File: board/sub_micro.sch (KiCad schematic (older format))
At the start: 2 parts, among them J301 USB_B, U301 STM32F072CBTx

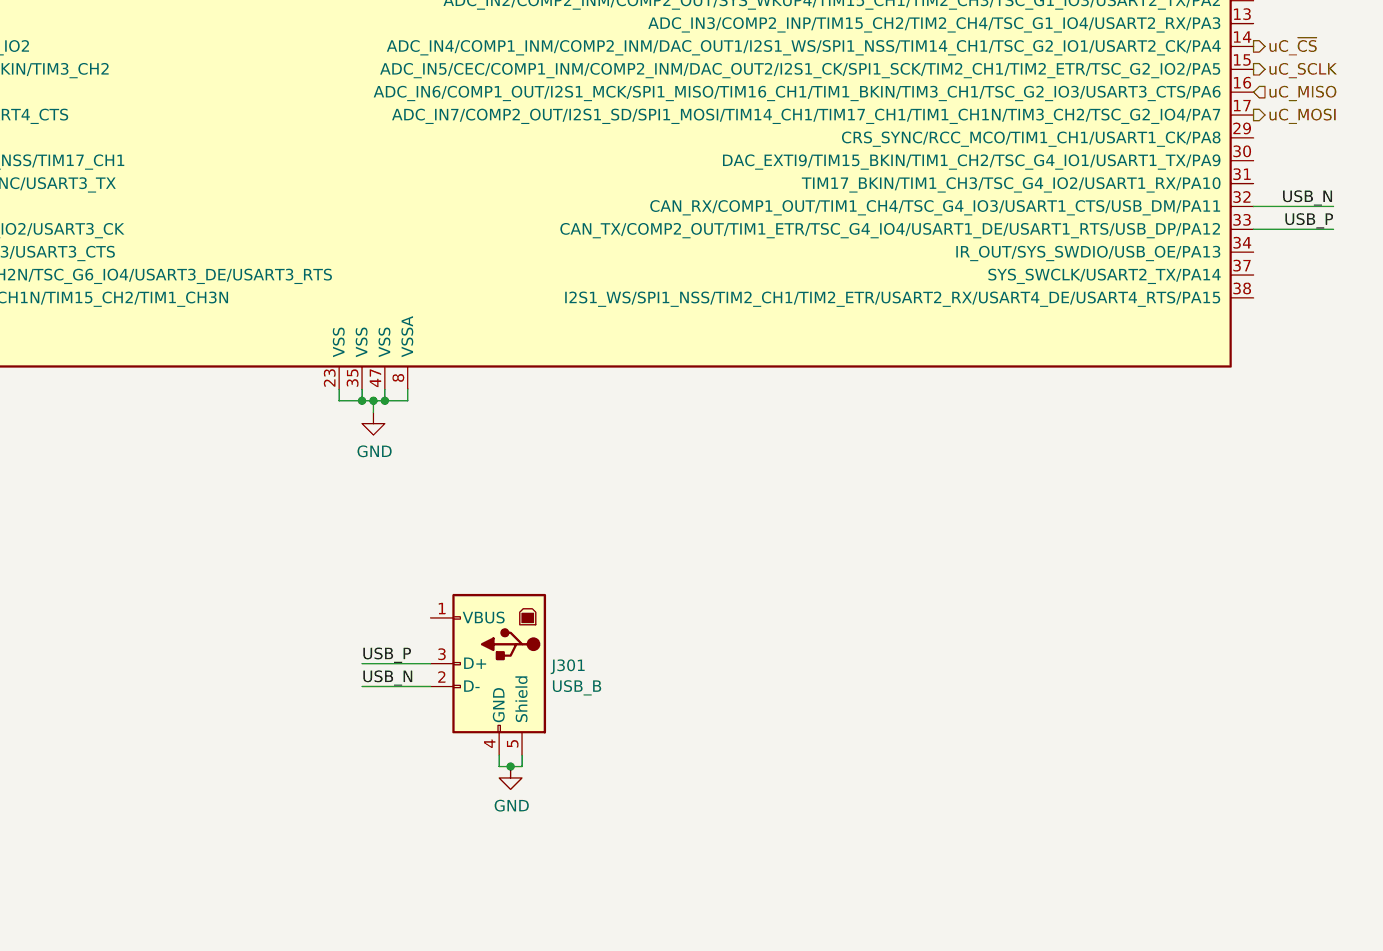
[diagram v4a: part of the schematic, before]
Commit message: made some changes based on projected power budget
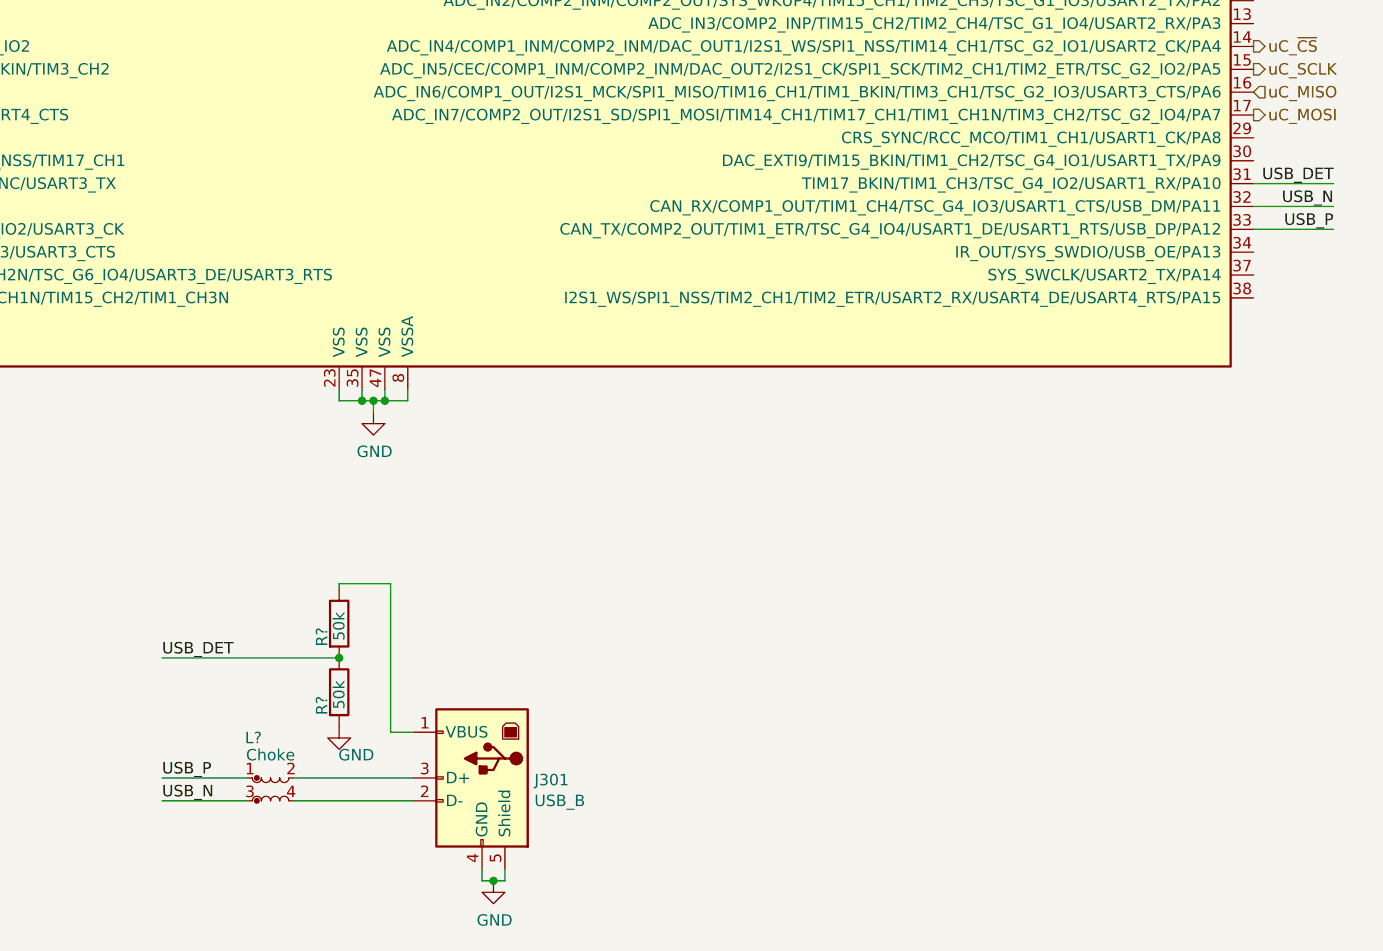
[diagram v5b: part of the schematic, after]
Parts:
- added L?: Choke, symbol Device:L_Coupled_Small
- added R? (x2): 50k, symbol Device:R
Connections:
- net GND: now also R?.2
- net USB_N: now also L?.3; no longer J301.2 (D-)
- net USB_P: now also L?.1; no longer J301.3 (D+)
- net USB_DET: now reaches U301.31 (TIM17_BKIN/TIM1_CH3/TSC_G4_IO2/USART1_RX/PA10)
- net USB_DET: now also R?.1, R?.2
- net at J301.1 (VBUS): now also R?.1
- new net: J301.2 (D-), L?.4
- new net: J301.3 (D+), L?.2
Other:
- moved on the sheet: J301
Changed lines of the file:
@@
 L Connector_Specialized:USB_B J301
 U 1 1 5AA35CDE
-P 5900 6150
-F 0 "J301" H 5671 6141 50  0000 R CNN
-F 1 "USB_B" H 5671 6050 50  0000 R CNN
-F 2 "" H 6050 6100 50  0001 C CNN
-F 3 "" H 6050 6100 50  0001 C CNN
-	1    5900 6150
+P 5825 6650
+F 0 "J301" H 5596 6641 50  0000 R CNN
+F 1 "USB_B" H 5596 6550 50  0000 R CNN
+F 2 "" H 5975 6600 50  0001 C CNN
+F 3 "" H 5975 6600 50  0001 C CNN
+	1    5825 6650
 	-1   0    0    -1
 $EndComp
@@
 Text Label 9550 4250 2    50   ~ 0
 USB_P
-Wire Wire Line
-	5600 6150 5300 6150
-Wire Wire Line
-	5600 6250 5300 6250
-Text Label 5300 6250 0    50   ~ 0
+Text Label 4425 6750 0    50   ~ 0
 USB_N
-Text Label 5300 6150 0    50   ~ 0
+Text Label 4425 6650 0    50   ~ 0
 USB_P
 $Comp
 L power:GND #PWR0303
 U 1 1 5AA58CA8
-P 5950 6600
-F 0 "#PWR0303" H 5950 6350 50  0001 C CNN
-F 1 "GND" H 5955 6427 50  0000 C CNN
-F 2 "" H 5950 6600 50  0001 C CNN
-F 3 "" H 5950 6600 50  0001 C CNN
-	1    5950 6600
+P 5875 7100
+F 0 "#PWR0303" H 5875 6850 50  0001 C CNN
+F 1 "GND" H 5880 6927 50  0000 C CNN
+F 2 "" H 5875 7100 50  0001 C CNN
+F 3 "" H 5875 7100 50  0001 C CNN
+	1    5875 7100
 	1    0    0    -1
 $EndComp
 Wire Wire Line
-	5900 6550 5900 6600
+	5825 7050 5825 7100
 Wire Wire Line
-	5900 6600 5950 6600
+	5825 7100 5875 7100
 Wire Wire Line
-	5950 6600 6000 6600
+	5875 7100 5925 7100
 Wire Wire Line
-	6000 6600 6000 6550
-Connection ~ 5950 6600
+	5925 7100 5925 7050
+Connection ~ 5875 7100
 $Comp
 L power:+2V5 #PWR0301
@@
 Text HLabel 1350 6500 2    50   Input ~ 0
 FPGA_INIT_B
+$Comp
+L Device:L_Coupled_Small L?
+U 1 1 5AC01C3F
+P 4900 6700
+F 0 "L?" H 4825 6925 50  0000 C CNN
+F 1 "Choke" H 4900 6850 50  0000 C CNN
+F 2 "" H 4900 6700 50  0001 C CNN
+F 3 "~" H 4900 6700 50  0001 C CNN
+	1    4900 6700
+	1    0    0    -1
+$EndComp
+Wire Wire Line
+	4425 6750 4800 6750
+Wire Wire Line
+	4425 6650 4800 6650
+Wire Wire Line
+	5000 6750 5525 6750
+Wire Wire Line
+	5000 6650 5525 6650
+$Comp
+L Device:R R?
+U 1 1 5AC07574
+P 5200 6275
+F 0 "R?" V 5125 6175 50  0000 L CNN
+F 1 "50k" V 5200 6200 50  0000 L CNN
+F 2 "" V 5130 6275 50  0001 C CNN
+F 3 "~" H 5200 6275 50  0001 C CNN
+	1    5200 6275
+	1    0    0    -1
+$EndComp
+$Comp
+L Device:R R?
+U 1 1 5AC078C2
+P 5200 5975
+F 0 "R?" V 5125 5875 50  0000 L CNN
+F 1 "50k" V 5200 5900 50  0000 L CNN
+F 2 "" V 5130 5975 50  0001 C CNN
+F 3 "~" H 5200 5975 50  0001 C CNN
+	1    5200 5975
+	1    0    0    -1
+$EndComp
+Wire Wire Line
+	5525 6450 5425 6450
+Wire Wire Line
+	5425 6450 5425 5800
+Wire Wire Line
+	5425 5800 5200 5800
+Wire Wire Line
+	5200 5800 5200 5825
+$Comp
+L power:GND #PWR?
+U 1 1 5AC0839F
+P 5200 6425
+F 0 "#PWR?" H 5200 6175 50  0001 C CNN
+F 1 "GND" H 5275 6300 50  0000 C CNN
+F 2 "" H 5200 6425 50  0001 C CNN
+F 3 "" H 5200 6425 50  0001 C CNN
+	1    5200 6425
+	1    0    0    -1
+$EndComp
+Wire Wire Line
+	5200 6125 4425 6125
+Connection ~ 5200 6125
+Text Label 4425 6125 0    50   ~ 0
+USB_DET
+Wire Wire Line
+	9200 4050 9550 4050
+Text Label 9550 4050 2    50   ~ 0
+USB_DET
 $EndSCHEMATC

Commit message: Schematics mostly complete
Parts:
- added C301, C302: 4.7u, symbol Device:C
- added C303: 1u, symbol Device:C
- added C304, C305, C306: 0.1u, symbol Device:C
- added C307: 10n, symbol Device:C
- added J301: ARM SWD, symbol Connector_Generic:Conn_02x05_Odd_Even
- added J302: Conn_01x02, symbol Connector_Generic:Conn_01x02
- added R301: 4.7k, symbol Device:R
- added U302: USBLC6-2SC6, Package_TO_SOT_SMD:SOT-23-6, symbol quokka:USBLC6-2SC6
- gave numbers to parts that had none: 3
- renumbered J301 to J303
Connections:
- net +2V5 is gone; now on net +3V3: U301.24 (VDD), U301.36 (VDDIO2), U301.48 (VDD), U301.9 (VDDA)
- net FPGA_DONE: now also U301.13 (ADC_IN3/COMP2_INP/TIM15_CH2/TIM2_CH4/TSC_G1_IO4/USART2_RX/PA3)
- net FPGA_INIT_B: now also U301.11 (ADC_IN1/COMP1_INP/TIM15_CH1N/TIM2_CH2/TSC_G1_IO2/USART2_DE/USART2_RTS/USART4_RX/PA1)
- net FPGA_PROG_B: now also U301.12 (ADC_IN2/COMP2_INM/COMP2_OUT/SYS_WKUP4/TIM15_CH1/TIM2_CH3/TSC_G1_IO3/USART2_TX/PA2)
- net FPGA_~INT: now also U301.10 (ADC_IN0/COMP1_INM/COMP1_OUT/RTC_TAMP2/SYS_WKUP1/TIM2_CH1/TIM2_ETR/TSC_G1_IO1/USART2_CTS/USART4_TX/PA0)
- net GND: now also C301.2, C302.2, C303.2, C304.2, C305.2, C306.2, C307.2, J301.3 (Pin_3), J301.5 (Pin_5), J301.9 (Pin_9), R301.2, U302.2 (GND)
- net +3V3: now reaches U301.1 (VBAT)
- net +3V3: now also C301.1, C302.1, C303.1, C304.1, C305.1, C306.1, C307.1, J301.1 (Pin_1), J302.2 (Pin_2)
- net SWDIO: now reaches U301.34 (IR_OUT/SYS_SWDIO/USB_OE/PA13)
- net SWDIO: now also J301.2 (Pin_2)
- net SWCLK: now reaches U301.37 (SYS_SWCLK/USART2_TX/PA14)
- net SWCLK: now also J301.4 (Pin_4)
- net at U301.44 (BOOT0): now also J302.1 (Pin_1), R301.1
- net NRST: now reaches U301.7 (NRST)
- net NRST: now also J301.10 (Pin_10)
- net at J303.1 (VBUS), R302.1: now also U302.5 (VBUS)
- net at J303.2 (D-): now also U302.4 (IO2); no longer L301.4
- net at J303.3 (D+): now also U302.6 (IO1); no longer L301.2
- new net: L301.2, U302.1 (IO1)
- new net: L301.4, U302.3 (IO2)
- no-connect marks 0 -> 25
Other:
- moved on the sheet: J303, L301, R302, R303, U301

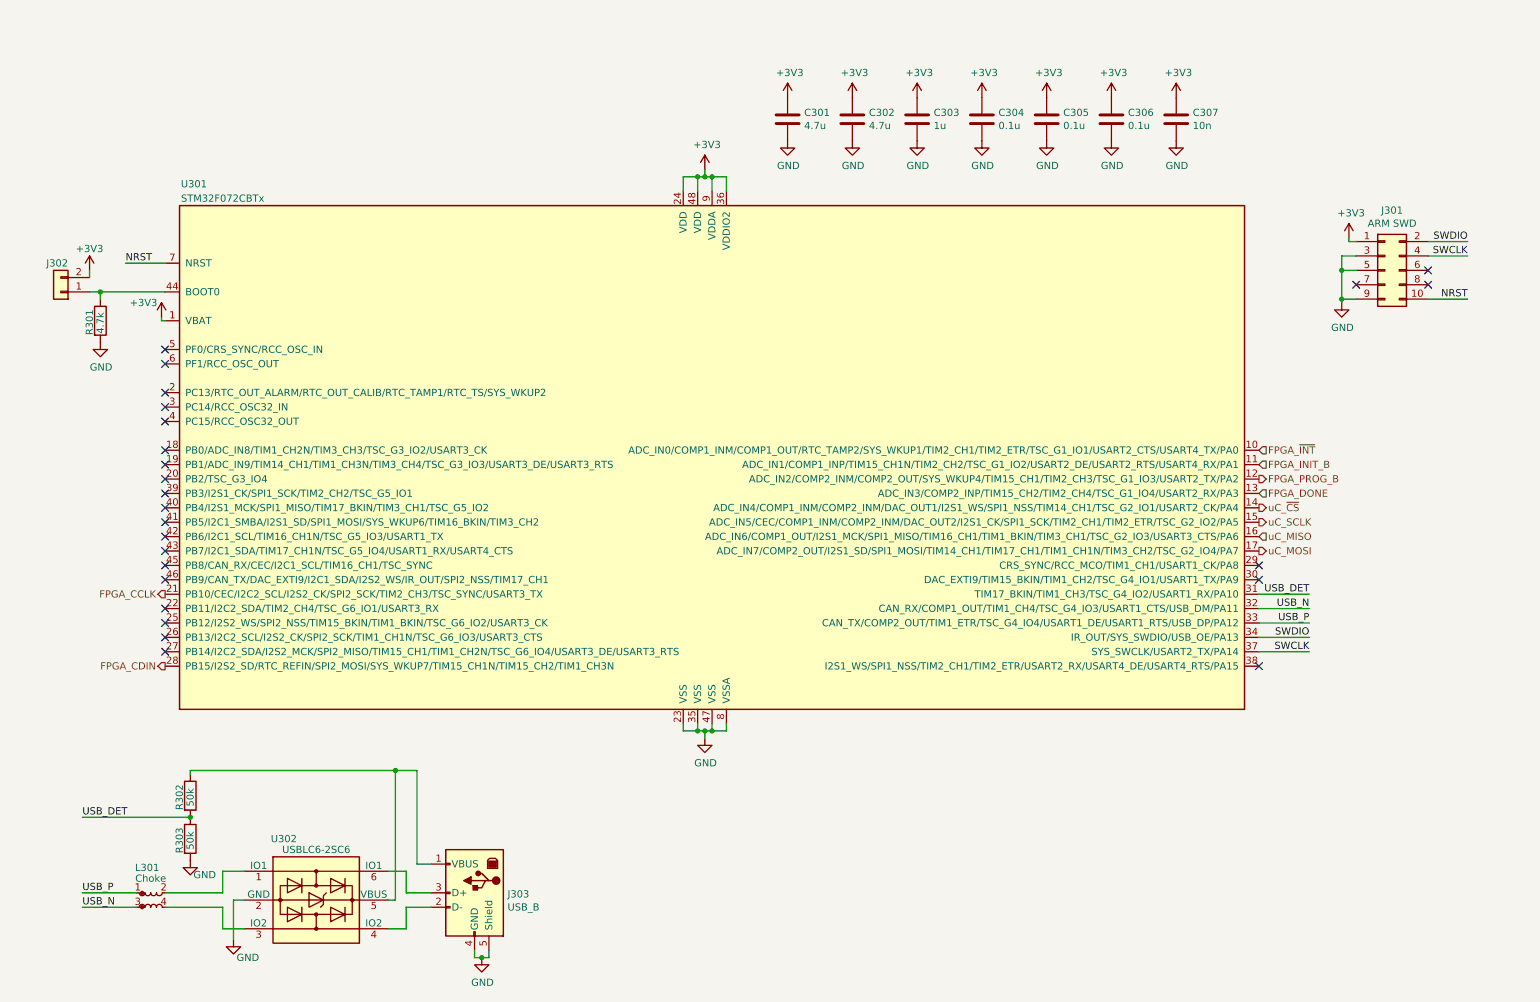
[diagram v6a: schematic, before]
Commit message: Started picking footprints. Merged many components.
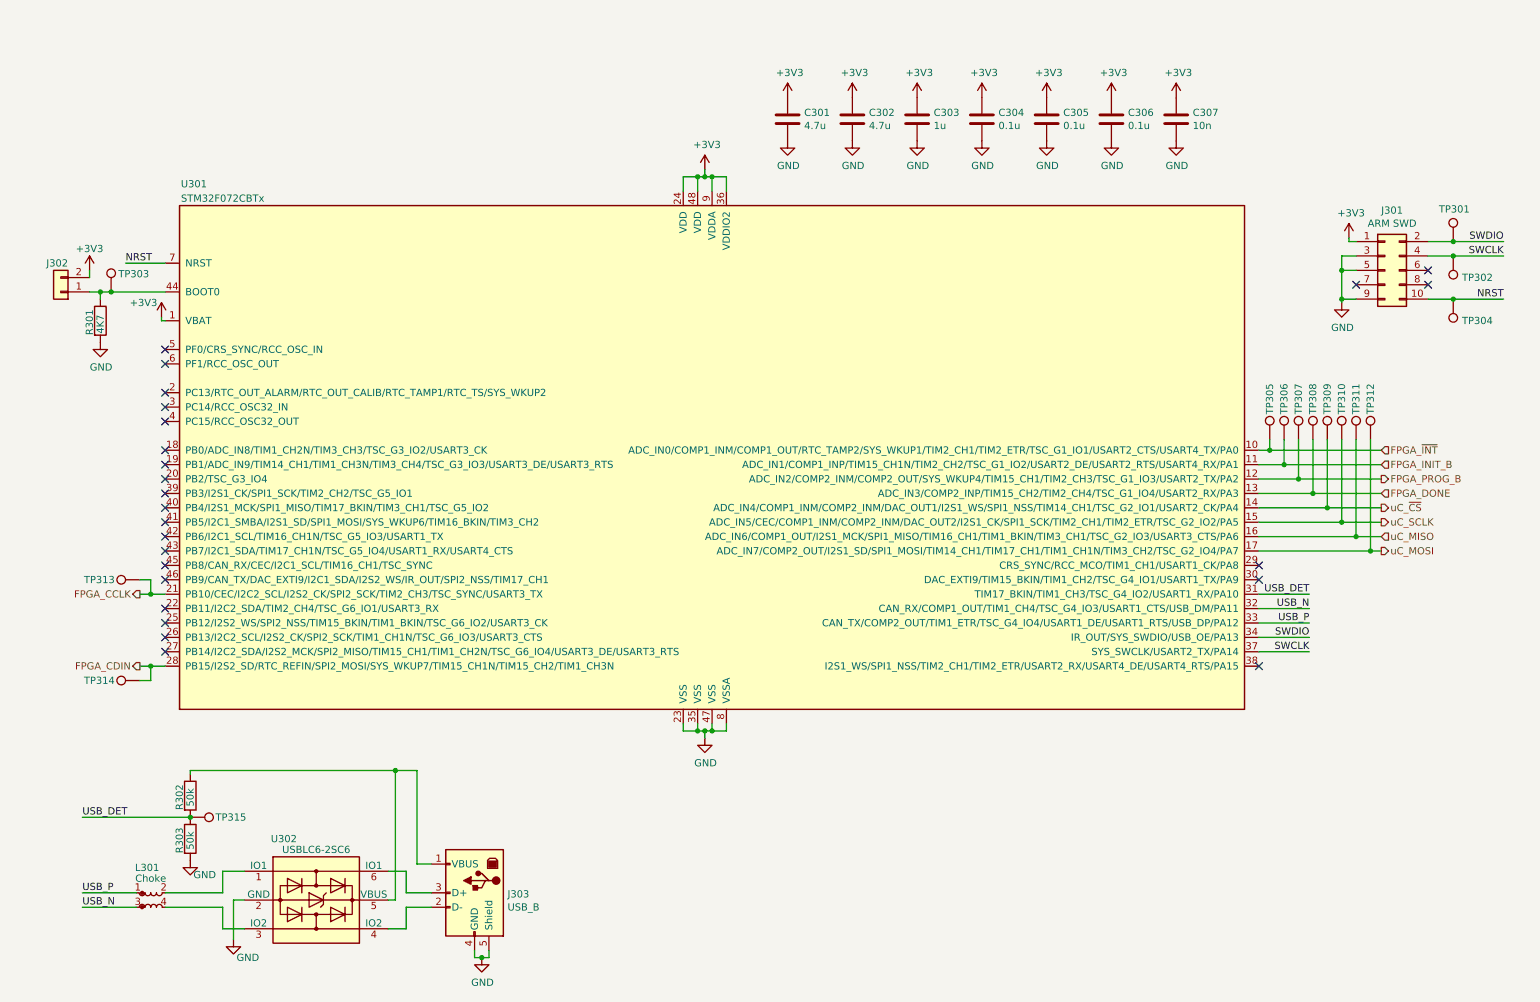
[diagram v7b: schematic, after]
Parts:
- added TP301, TP302, TP303, TP304, TP305, TP306, TP307, TP308, TP309, TP310, TP311, TP312, TP313, TP314, TP315: Test_Point, TestPoint:TestPoint_Plated_Hole_D2.0mm, symbol Connector_Specialized:Test_Point
- R301: value 4.7k -> 4K7
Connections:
- net FPGA_CCLK: now also TP313.1
- net FPGA_CDIN: now also TP314.1
- net FPGA_DONE: now also TP308.1
- net FPGA_INIT_B: now also TP306.1
- net FPGA_PROG_B: now also TP307.1
- net FPGA_~INT: now also TP305.1
- net NRST: now also TP304.1
- net SWCLK: now also TP302.1
- net SWDIO: now also TP301.1
- net USB_DET: now also TP315.1
- net uC_MISO: now also TP311.1
- net uC_MOSI: now also TP312.1
- net uC_SCLK: now also TP310.1
- net uC_~CS: now also TP309.1
- net at J302.1 (Pin_1), R301.1, U301.44 (BOOT0): now also TP303.1

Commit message: More footprints done. Went with simpler test-pads.
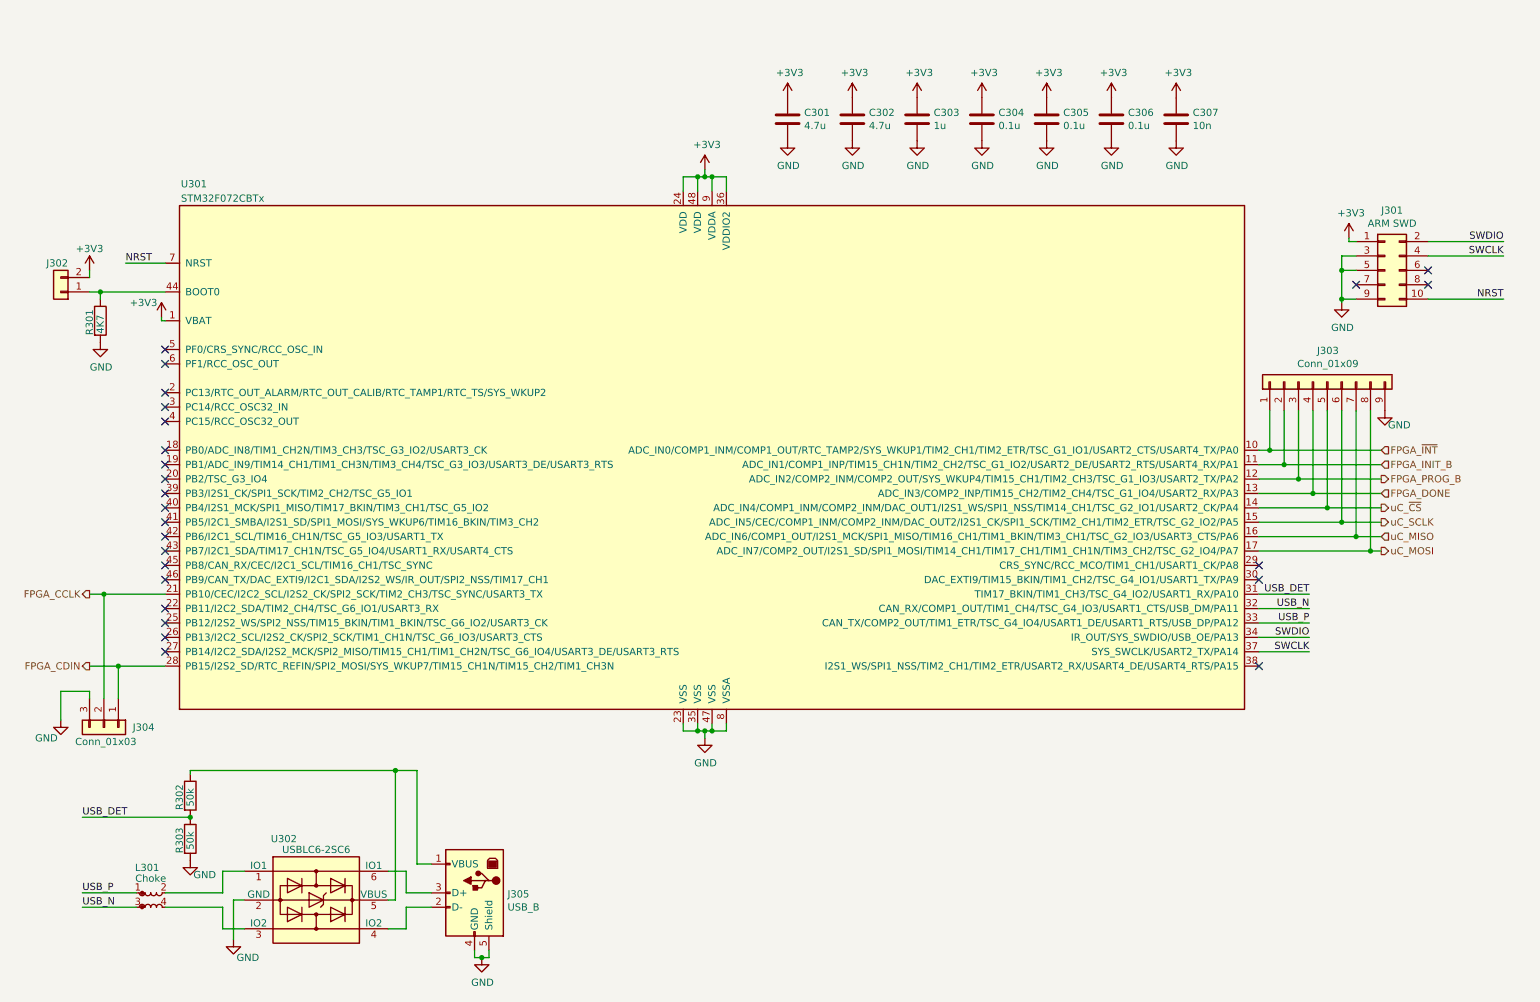
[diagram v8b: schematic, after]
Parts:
- removed TP301, TP302, TP303, TP304, TP305, TP306, TP307, TP308, TP309, TP310, TP311, TP312, TP313, TP314, TP315: Test_Point, TestPoint:TestPoint_Plated_Hole_D2.0mm, symbol Connector_Specialized:Test_Point
- added J303: Conn_01x09, symbol Connector_Generic:Conn_01x09
- added J304: Conn_01x03, symbol Connector_Generic:Conn_01x03
- J301: footprint (none) -> Connector_PinHeader_1.27mm:PinHeader_2x05_P1.27mm_Vertical_SMD
- J302: footprint (none) -> Connector_PinHeader_2.54mm:PinHeader_1x02_P2.54mm_Vertical
- renumbered J303 to J305
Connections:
- net FPGA_CCLK: now also J304.2 (Pin_2)
- net FPGA_CDIN: now also J304.1 (Pin_1)
- net FPGA_DONE: now also J303.4 (Pin_4)
- net FPGA_INIT_B: now also J303.2 (Pin_2)
- net FPGA_PROG_B: now also J303.3 (Pin_3)
- net FPGA_~INT: now also J303.1 (Pin_1)
- net GND: now also J303.9 (Pin_9), J304.3 (Pin_3)
- net uC_MISO: now also J303.7 (Pin_7)
- net uC_MOSI: now also J303.8 (Pin_8)
- net uC_SCLK: now also J303.6 (Pin_6)
- net uC_~CS: now also J303.5 (Pin_5)
